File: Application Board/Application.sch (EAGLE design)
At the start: 54 parts, among them Q1 DMP2012SN-7, T1 FDN340P, T2 AP1117_LIN_REG, U1 LM3409HV'LM3409HV', X1 22-23-2101

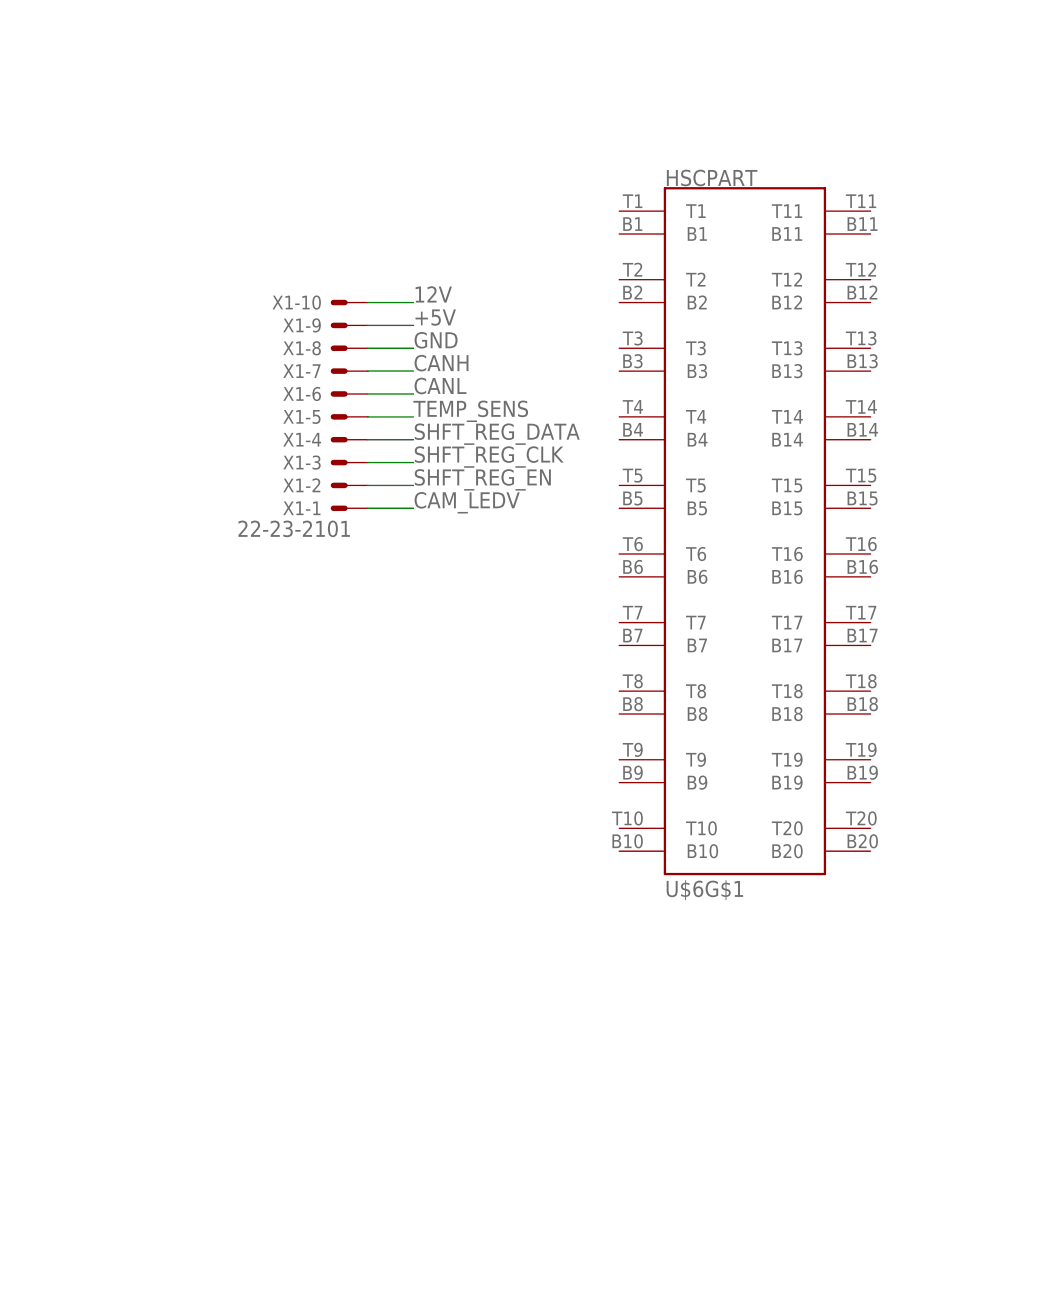
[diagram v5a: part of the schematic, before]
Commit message: Fixed output voltages and signal paths, added connector
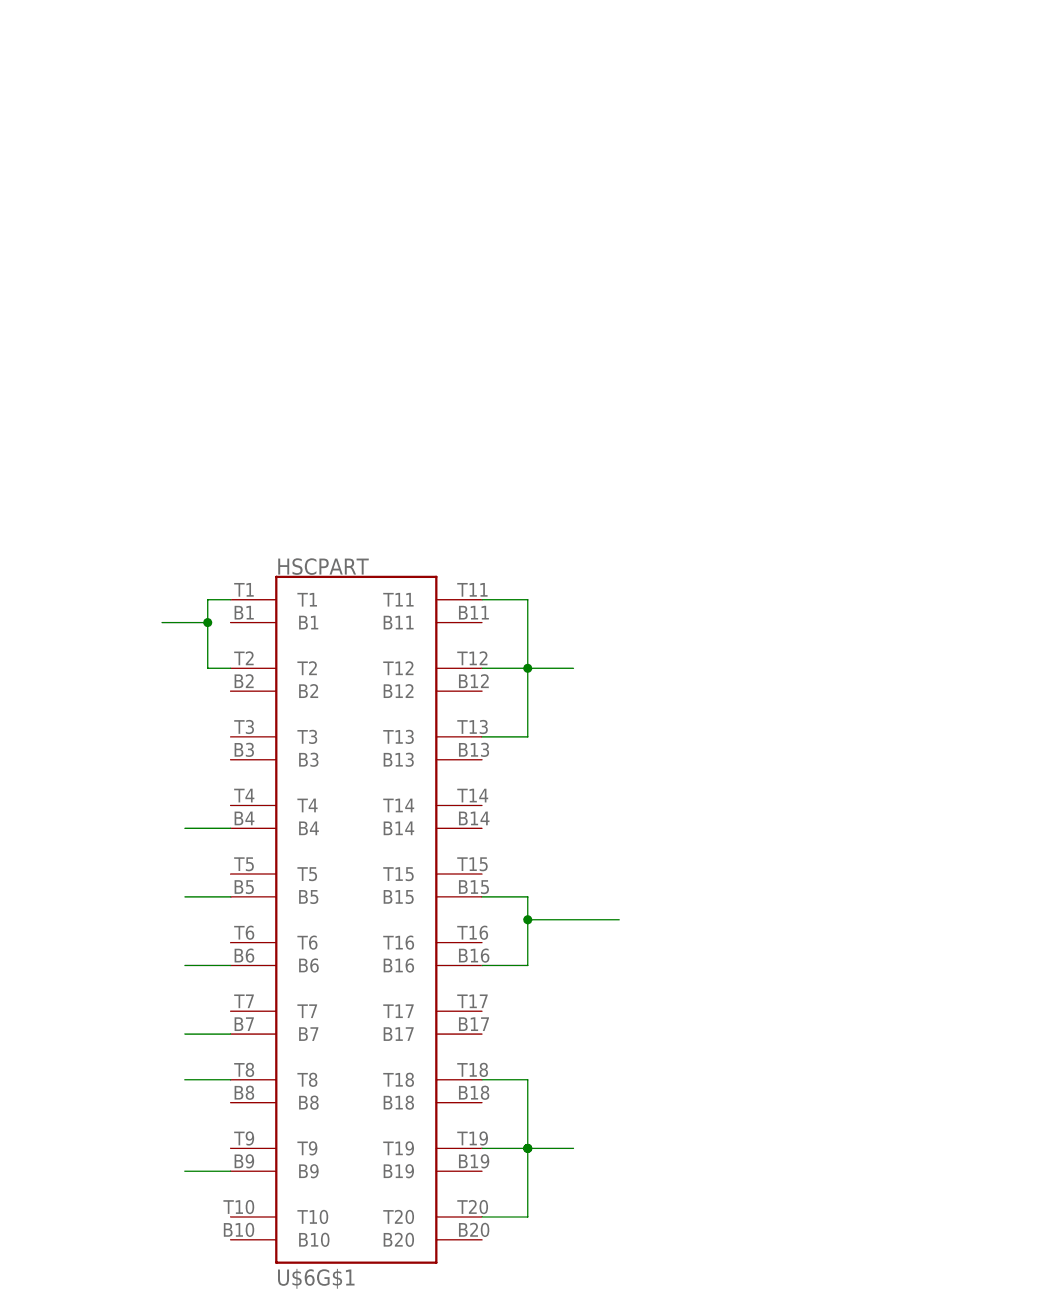
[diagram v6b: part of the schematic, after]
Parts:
- removed X1: 22-23-2101, con-molex:22-23-2101
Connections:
- net +5V: now also U$6G$1.B15, U$6G$1.B16; no longer X1-9.S
- net 12V: now also U$6G$1.T18, U$6G$1.T19, U$6G$1.T20; no longer X1-10.S
- net CAM_LEDV: now also U$6G$1.T1, U$6G$1.T2; no longer X1-1.S
- net CANH: now also U$6G$1.B9; no longer X1-7.S
- net CANL: now also U$6G$1.B7; no longer X1-6.S
- net GND: now also U$6G$1.T11, U$6G$1.T12, U$6G$1.T13; no longer X1-8.S
- net SHFT_REG_CLK: now also U$6G$1.B4; no longer X1-3.S
- net SHFT_REG_DATA: now also U$6G$1.B6; no longer X1-4.S
- net SHFT_REG_EN: now also U$6G$1.B5; no longer X1-2.S
- net TEMP_SENS: now also U$6G$1.T8; no longer X1-5.S
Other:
- moved on the sheet: U$6G$1
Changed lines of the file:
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@@
 <part name="U1" library="2015_LED_Driver" deviceset="LM3409HV" device="'LM3409HV'"/>
 <part name="FRAME3" library="frames" deviceset="FRAME_A_L" device=""/>
-<part name="X1" library="con-molex" deviceset="22-23-2101" device=""/>
 <part name="U$6" library="Connectors" deviceset="HSCPART" device=""/>
 </parts>
@@
 <instance part="FRAME3" gate="G$1" x="-27.94" y="-243.84"/>
 <instance part="FRAME3" gate="G$2" x="139.7" y="-243.84"/>
-<instance part="X1" gate="-1" x="180.34" y="-121.92" rot="R180"/>
-<instance part="X1" gate="-2" x="180.34" y="-119.38" rot="R180"/>
-<instance part="X1" gate="-3" x="180.34" y="-116.84" rot="R180"/>
-<instance part="X1" gate="-4" x="180.34" y="-114.3" rot="R180"/>
-<instance part="X1" gate="-5" x="180.34" y="-111.76" rot="R180"/>
-<instance part="X1" gate="-6" x="180.34" y="-109.22" rot="R180"/>
-<instance part="X1" gate="-7" x="180.34" y="-106.68" rot="R180"/>
-<instance part="X1" gate="-8" x="180.34" y="-104.14" rot="R180"/>
-<instance part="X1" gate="-9" x="180.34" y="-101.6" rot="R180"/>
-<instance part="X1" gate="-10" x="180.34" y="-99.06" rot="R180"/>
-<instance part="U$6" gate="G$1" x="223.52" y="-111.76"/>
+<instance part="U$6" gate="G$1" x="180.34" y="-154.94"/>
 </instances>
 <busses>
@@
 </segment>
 <segment>
-<pinref part="X1" gate="-8" pin="S"/>
-<wire x1="182.88" y1="-104.14" x2="187.96" y2="-104.14" width="0.1524" layer="91"/>
-<label x="187.96" y="-104.14" size="1.778" layer="95"/>
+<pinref part="U$6" gate="G$1" pin="T12"/>
+<wire x1="195.58" y1="-139.7" x2="200.66" y2="-139.7" width="0.1524" layer="91"/>
+<wire x1="200.66" y1="-139.7" x2="200.66" y2="-132.08" width="0.1524" layer="91"/>
+<pinref part="U$6" gate="G$1" pin="T11"/>
+<wire x1="200.66" y1="-132.08" x2="195.58" y2="-132.08" width="0.1524" layer="91"/>
+<pinref part="U$6" gate="G$1" pin="T13"/>
+<wire x1="195.58" y1="-147.32" x2="200.66" y2="-147.32" width="0.1524" layer="91"/>
+<wire x1="200.66" y1="-147.32" x2="200.66" y2="-139.7" width="0.1524" layer="91"/>
+<junction x="200.66" y="-139.7"/>
+<wire x1="200.66" y1="-139.7" x2="205.74" y2="-139.7" width="0.1524" layer="91"/>
 </segment>
 </net>
@@
 </segment>
 <segment>
-<pinref part="X1" gate="-9" pin="S"/>
-<wire x1="182.88" y1="-101.6" x2="187.96" y2="-101.6" width="0.1524" layer="91"/>
-<label x="187.96" y="-101.6" size="1.778" layer="95"/>
+<pinref part="U$6" gate="G$1" pin="B16"/>
+<wire x1="195.58" y1="-172.72" x2="200.66" y2="-172.72" width="0.1524" layer="91"/>
+<wire x1="200.66" y1="-172.72" x2="200.66" y2="-167.64" width="0.1524" layer="91"/>
+<pinref part="U$6" gate="G$1" pin="B15"/>
+<wire x1="200.66" y1="-167.64" x2="200.66" y2="-165.1" width="0.1524" layer="91"/>
+<wire x1="200.66" y1="-165.1" x2="195.58" y2="-165.1" width="0.1524" layer="91"/>
+<wire x1="200.66" y1="-167.64" x2="210.82" y2="-167.64" width="0.1524" layer="91"/>
+<junction x="200.66" y="-167.64"/>
 </segment>
 </net>
@@
 </segment>
 <segment>
-<pinref part="X1" gate="-6" pin="S"/>
-<wire x1="182.88" y1="-109.22" x2="187.96" y2="-109.22" width="0.1524" layer="91"/>
-<label x="187.96" y="-109.22" size="1.778" layer="95"/>
+<pinref part="U$6" gate="G$1" pin="B7"/>
+<wire x1="162.56" y1="-180.34" x2="167.64" y2="-180.34" width="0.1524" layer="91"/>
 </segment>
 </net>
@@
 </segment>
 <segment>
-<pinref part="X1" gate="-7" pin="S"/>
-<wire x1="182.88" y1="-106.68" x2="187.96" y2="-106.68" width="0.1524" layer="91"/>
-<label x="187.96" y="-106.68" size="1.778" layer="95"/>
+<pinref part="U$6" gate="G$1" pin="B9"/>
+<wire x1="162.56" y1="-195.58" x2="167.64" y2="-195.58" width="0.1524" layer="91"/>
 </segment>
 </net>
@@
 </segment>
 <segment>
-<pinref part="X1" gate="-4" pin="S"/>
-<wire x1="182.88" y1="-114.3" x2="187.96" y2="-114.3" width="0.1524" layer="91"/>
-<label x="187.96" y="-114.3" size="1.778" layer="95"/>
+<pinref part="U$6" gate="G$1" pin="B6"/>
+<wire x1="167.64" y1="-172.72" x2="162.56" y2="-172.72" width="0.1524" layer="91"/>
 </segment>
 </net>
@@
 </segment>
 <segment>
-<pinref part="X1" gate="-3" pin="S"/>
-<wire x1="182.88" y1="-116.84" x2="187.96" y2="-116.84" width="0.1524" layer="91"/>
-<label x="187.96" y="-116.84" size="1.778" layer="95"/>
+<pinref part="U$6" gate="G$1" pin="B4"/>
+<wire x1="162.56" y1="-157.48" x2="167.64" y2="-157.48" width="0.1524" layer="91"/>
 </segment>
 </net>
@@
 </segment>
 <segment>
-<pinref part="X1" gate="-2" pin="S"/>
-<wire x1="182.88" y1="-119.38" x2="187.96" y2="-119.38" width="0.1524" layer="91"/>
-<label x="187.96" y="-119.38" size="1.778" layer="95"/>
+<pinref part="U$6" gate="G$1" pin="B5"/>
+<wire x1="167.64" y1="-165.1" x2="162.56" y2="-165.1" width="0.1524" layer="91"/>
 </segment>
 </net>
@@
 </segment>
 <segment>
-<pinref part="X1" gate="-5" pin="S"/>
-<wire x1="182.88" y1="-111.76" x2="187.96" y2="-111.76" width="0.1524" layer="91"/>
-<label x="187.96" y="-111.76" size="1.778" layer="95"/>
+<pinref part="U$6" gate="G$1" pin="T8"/>
+<wire x1="167.64" y1="-185.42" x2="162.56" y2="-185.42" width="0.1524" layer="91"/>
 </segment>
 </net>
@@
 </segment>
 <segment>
-<pinref part="X1" gate="-1" pin="S"/>
-<wire x1="182.88" y1="-121.92" x2="187.96" y2="-121.92" width="0.1524" layer="91"/>
-<label x="187.96" y="-121.92" size="1.778" layer="95"/>
+<pinref part="U$6" gate="G$1" pin="T2"/>
+<wire x1="167.64" y1="-139.7" x2="165.1" y2="-139.7" width="0.1524" layer="91"/>
+<wire x1="165.1" y1="-139.7" x2="165.1" y2="-134.62" width="0.1524" layer="91"/>
+<pinref part="U$6" gate="G$1" pin="T1"/>
+<wire x1="165.1" y1="-134.62" x2="165.1" y2="-132.08" width="0.1524" layer="91"/>
+<wire x1="165.1" y1="-132.08" x2="167.64" y2="-132.08" width="0.1524" layer="91"/>
+<wire x1="165.1" y1="-134.62" x2="160.02" y2="-134.62" width="0.1524" layer="91"/>
+<junction x="165.1" y="-134.62"/>
 </segment>
 </net>
@@
 </net>
 <net name="12V" class="0">
-<segment>
-<pinref part="X1" gate="-10" pin="S"/>
-<wire x1="182.88" y1="-99.06" x2="187.96" y2="-99.06" width="0.1524" layer="91"/>
-<label x="187.96" y="-99.06" size="1.778" layer="95"/>
-</segment>
 <segment>
 <pinref part="C_F" gate="G$1" pin="1"/>
@@
 <junction x="91.44" y="-133.35"/>
 </segment>
-</net>
+<segment>
+<pinref part="U$6" gate="G$1" pin="T20"/>
+<wire x1="195.58" y1="-200.66" x2="200.66" y2="-200.66" width="0.1524" layer="91"/>
+<wire x1="200.66" y1="-200.66" x2="200.66" y2="-193.04" width="0.1524" layer="91"/>
+<wire x1="200.66" y1="-193.04" x2="200.66" y2="-185.42" width="0.1524" layer="91"/>
+<pinref part="U$6" gate="G$1" pin="T19"/>
+<wire x1="195.58" y1="-193.04" x2="200.66" y2="-193.04" width="0.1524" layer="91"/>
+<junction x="200.66" y="-193.04"/>
+<pinref part="U$6" gate="G$1" pin="T18"/>
+<wire x1="195.58" y1="-185.42" x2="200.66" y2="-185.42" width="0.1524" layer="91"/>
+<wire x1="200.66" y1="-193.04" x2="205.74" y2="-193.04" width="0.1524" layer="91"/>
+<junction x="200.66" y="-193.04"/>
+</segment>
+</net>

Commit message: Fixed up some wiring
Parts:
- removed U$6: HSCPART, Connectors:HSCPART
- added U$2: HSCPART, Connectors:HSCPART
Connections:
- removed net 12V: C_F.1, C_IN1.1, C_IN2.1, R_SNS.2, R_UV2.2, U$6G$1.T18, U$6G$1.T19, U$6G$1.T20, U1.CSP, U1.VIN
- new net +12V: C_F.1, C_IN1.1, C_IN2.1, R_SNS.2, R_UV2.2, U$2G$1.T10, U$2G$1.T11, U$2G$1.T12, U$2G$1.T13, U$2G$1.T7, U$2G$1.T8, U$2G$1.T9, U1.CSP, U1.VIN
- net +3V3: now also U$2G$2.B24
- net +5V: now also U$2G$1.B1, U$2G$1.B2, U$2G$1.B3, U$2G$1.B4, U$2G$1.B5, U$2G$1.B6; no longer U$6G$1.B15, U$6G$1.B16
- net CAM_LEDV: no longer U$6G$1.T1, U$6G$1.T2
- net CANH: now also U$2G$2.B35; no longer U$6G$1.B9
- net CANL: now also U$2G$2.B33; no longer U$6G$1.B7
- net GND: now also U$2G$1.T14, U$2G$1.T15, U$2G$1.T16, U$2G$1.T17, U$2G$1.T18, U$2G$1.T19, U$2G$1.T20; no longer U$6G$1.T11, U$6G$1.T12, U$6G$1.T13
- net SHFT_REG_CLK: no longer U$6G$1.B4
- net SHFT_REG_DATA: no longer U$6G$1.B6
- net SHFT_REG_EN: no longer U$6G$1.B5
- net TEMP_SENS: now also U$2G$2.B25; no longer U$6G$1.T8

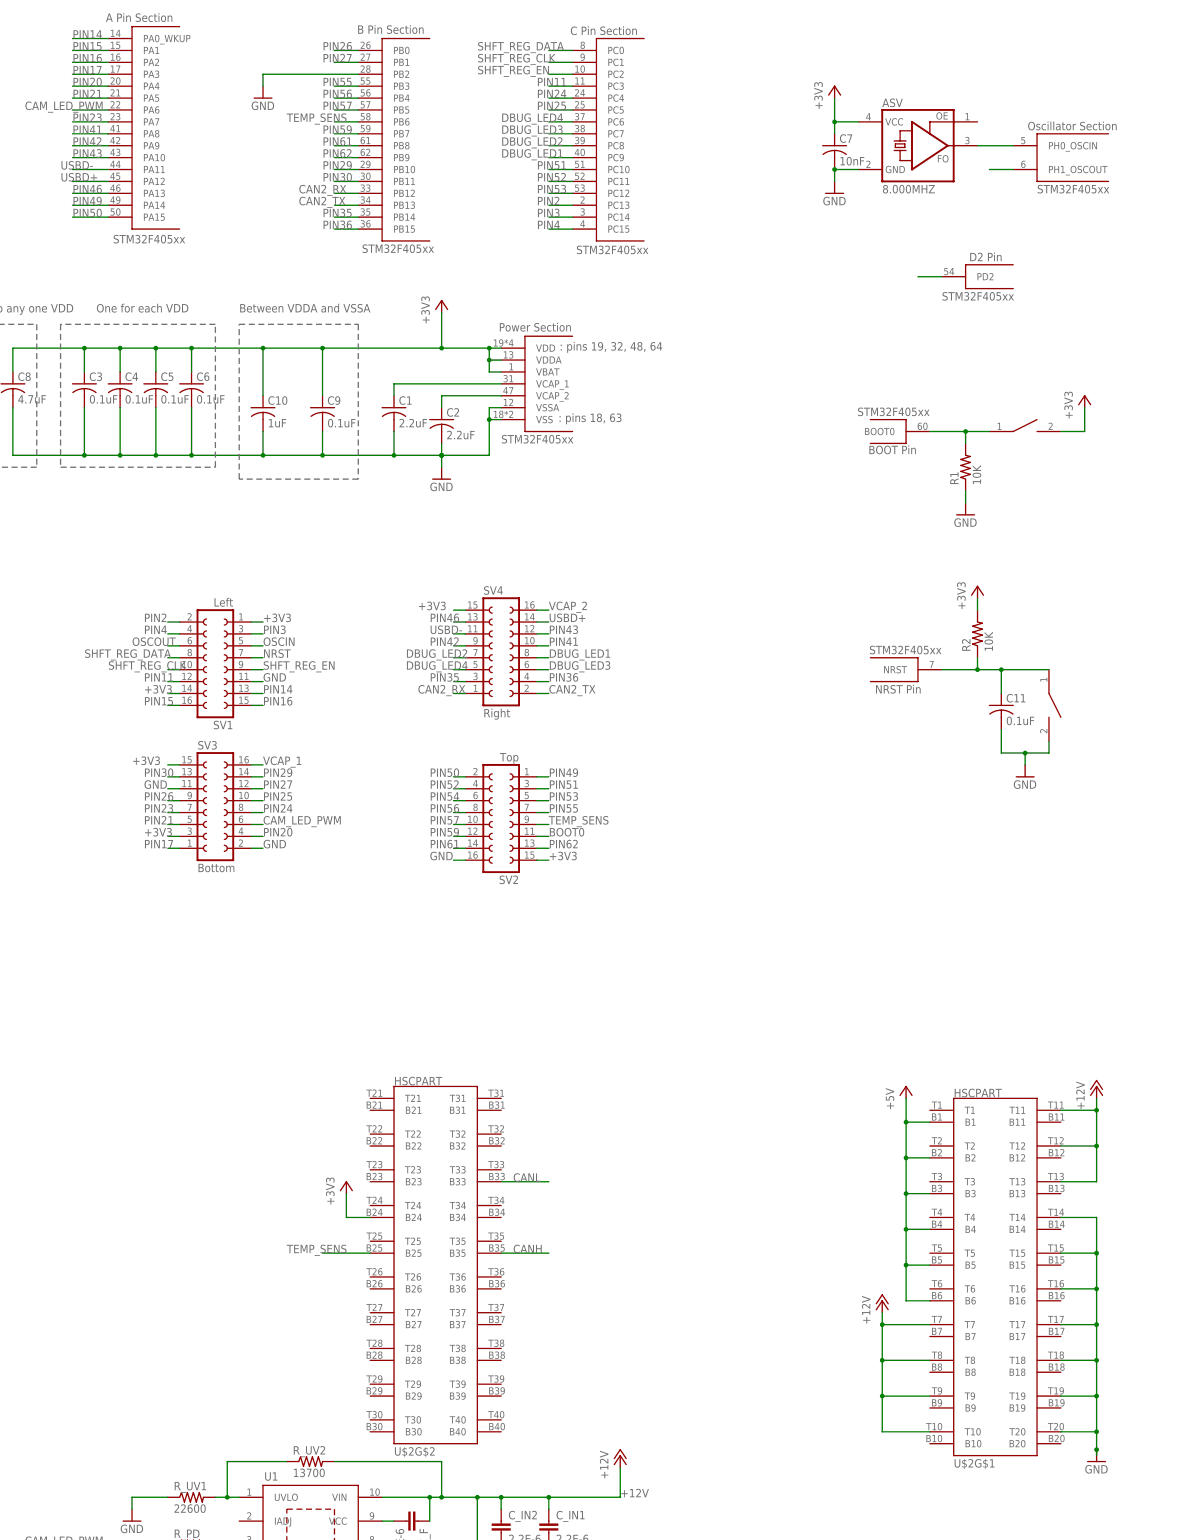
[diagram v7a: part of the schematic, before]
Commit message: fixed some connections
Have been trying to solve some problems with some polygons and haven't
been able to fix other issues.
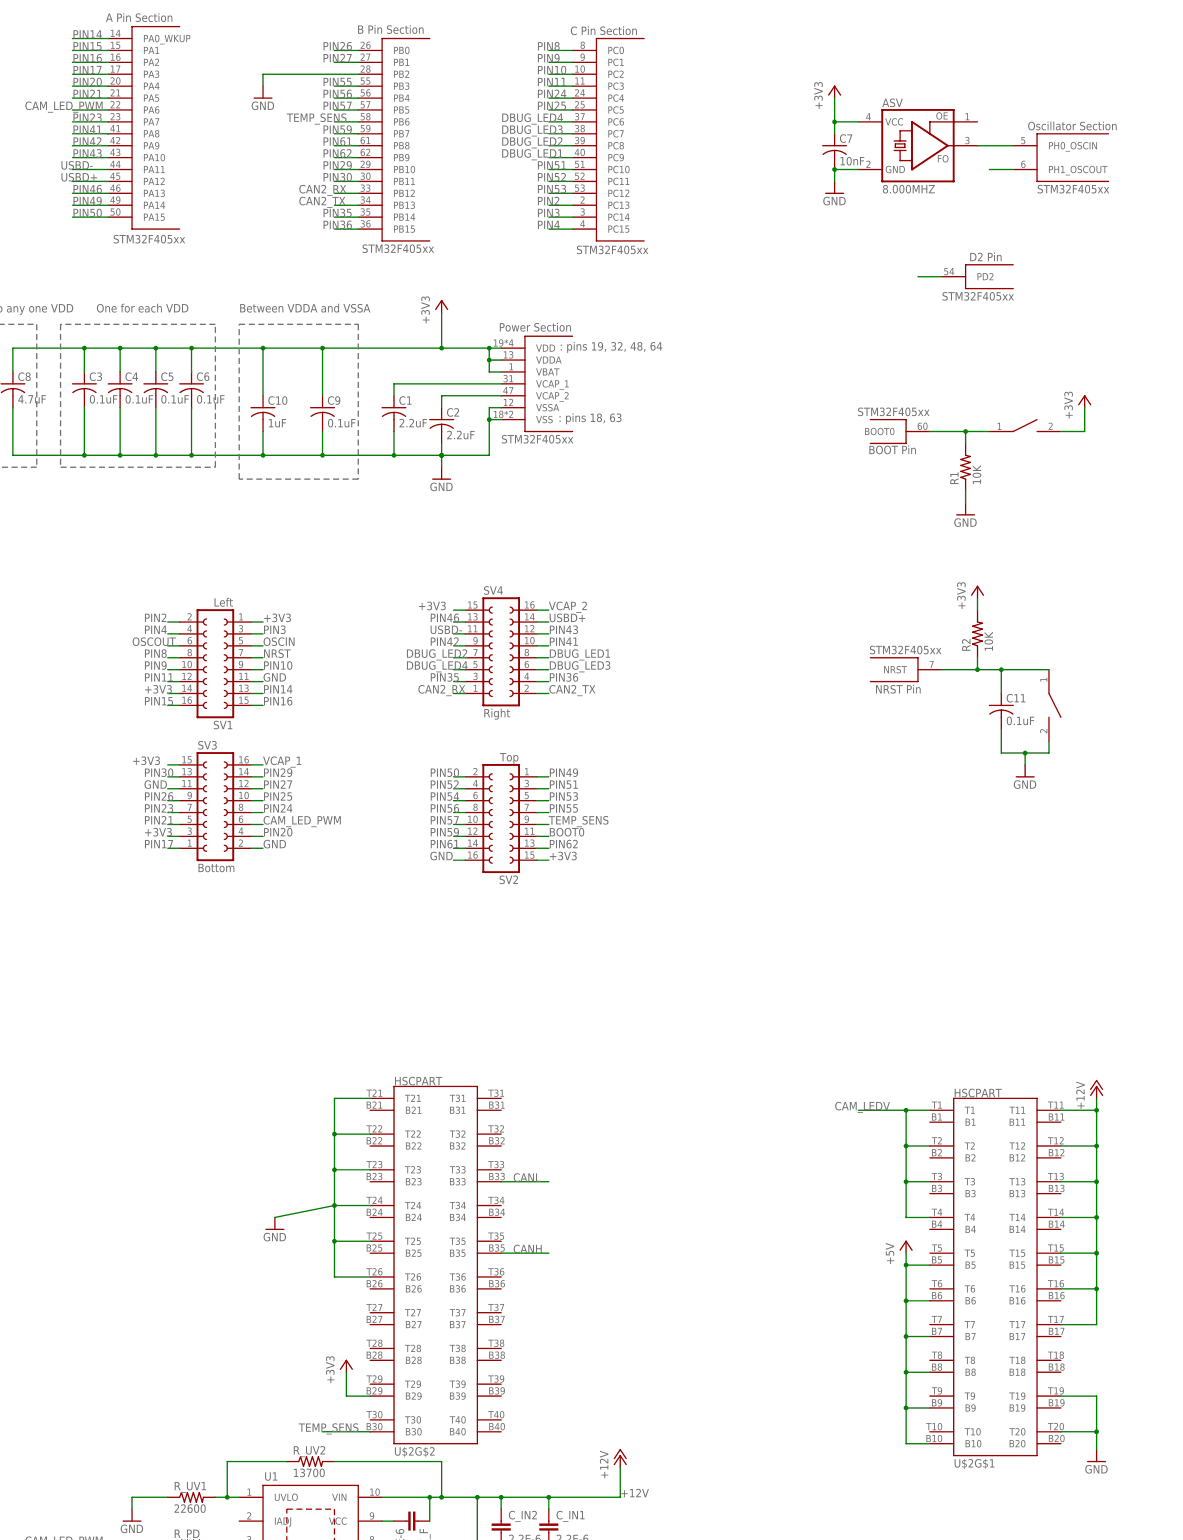
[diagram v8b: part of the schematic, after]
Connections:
- net SHFT_REG_CLK renamed PIN9
- net SHFT_REG_DATA renamed PIN8
- net SHFT_REG_EN renamed PIN10
- net +12V: now also U$2G$1.T14, U$2G$1.T15, U$2G$1.T16, U$2G$1.T17; no longer U$2G$1.T10, U$2G$1.T7, U$2G$1.T8, U$2G$1.T9
- net +3V3: now also U$2G$2.B29; no longer U$2G$2.B24
- net +5V: now also U$2G$1.B10, U$2G$1.B7, U$2G$1.B8, U$2G$1.B9; no longer U$2G$1.B1, U$2G$1.B2, U$2G$1.B3, U$2G$1.B4
- net CAM_LEDV: now also U$2G$1.T1, U$2G$1.T2, U$2G$1.T3, U$2G$1.T4
- net GND: now also U$2G$2.T21, U$2G$2.T22, U$2G$2.T23, U$2G$2.T24, U$2G$2.T25, U$2G$2.T26; no longer U$2G$1.T14, U$2G$1.T15, U$2G$1.T16, U$2G$1.T17, U$2G$1.T18
- net TEMP_SENS: now also U$2G$2.B30; no longer U$2G$2.B25
